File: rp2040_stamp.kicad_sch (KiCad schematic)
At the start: 38 parts, among them J1 Conn_South, J2 Conn_North, J3 Conn_East, J4 Conn_West, Q1 BSS84, SW1 SW_RESET, U1 RP2040, U2 AP2112K-3.3, U3 W25Q64JV, U4 MCP73831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

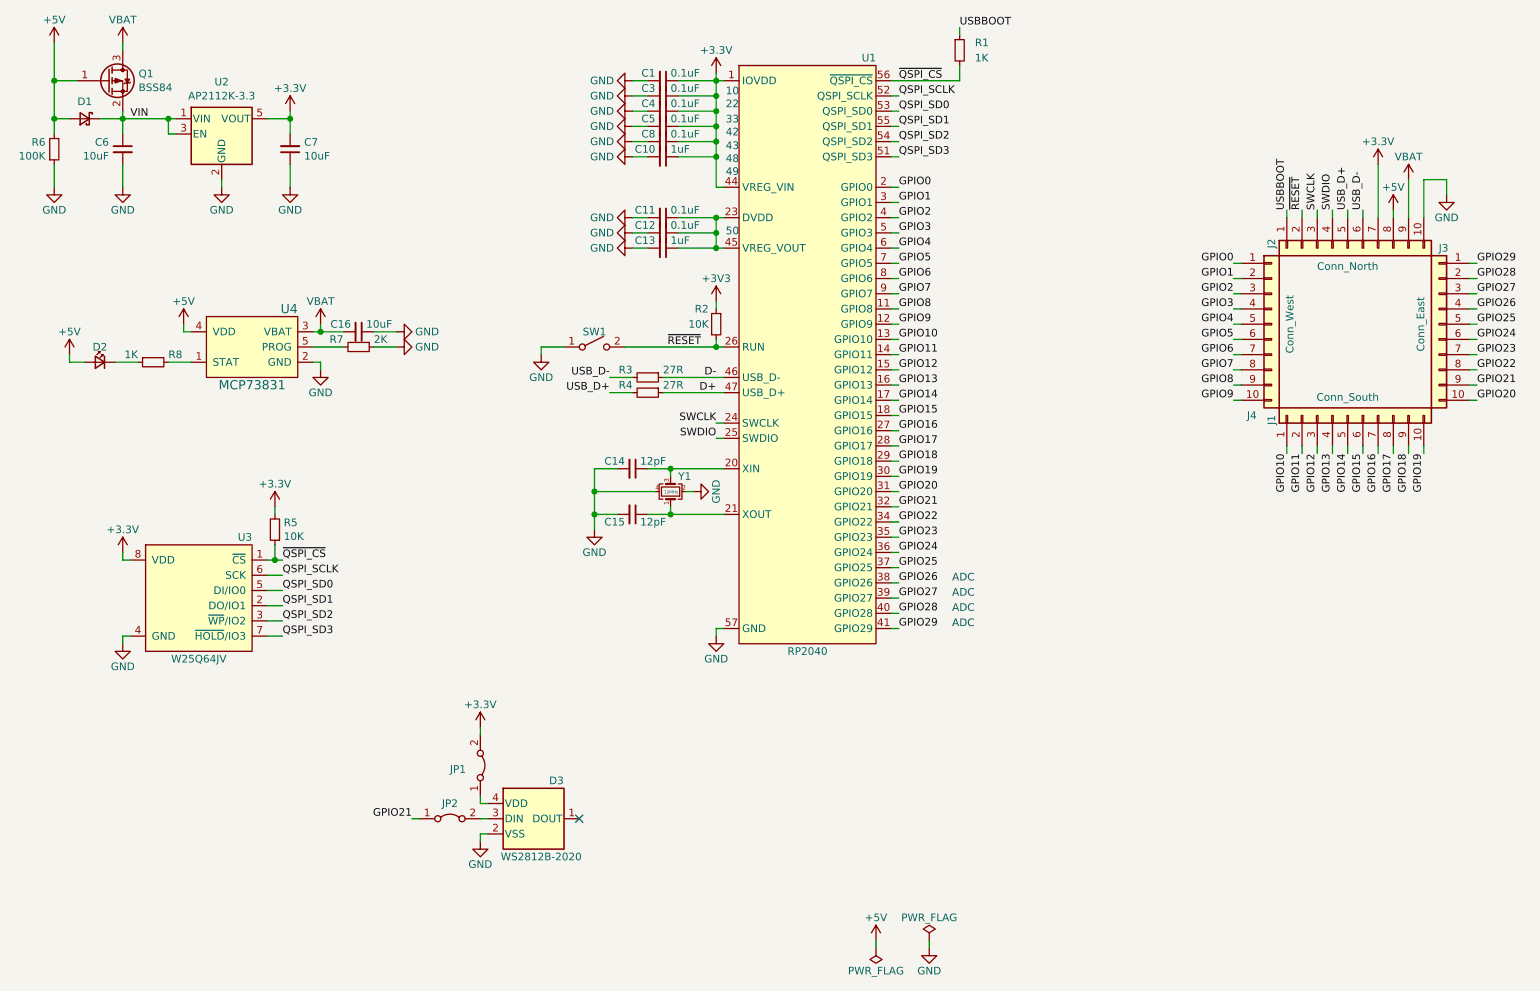
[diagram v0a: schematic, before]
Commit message: Removed unnecessary parts to be cheaper to manufacture via JLC.
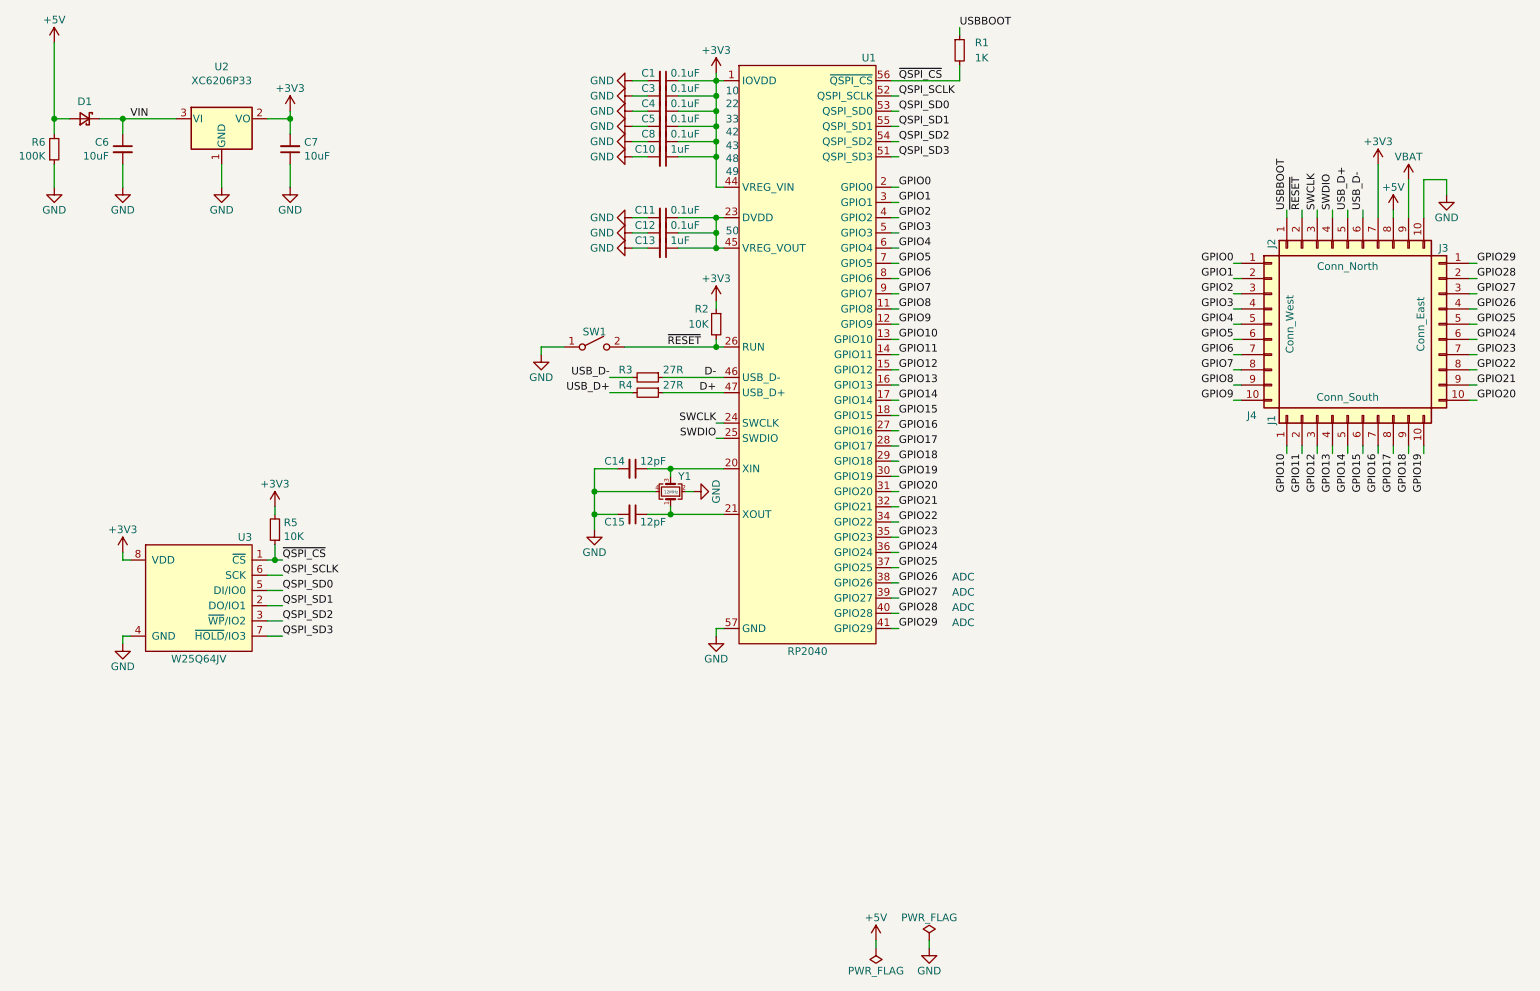
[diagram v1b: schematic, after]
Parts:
- removed C16: 10uF, Capacitor_SMD:C_0603_1608Metric, symbol Device:C_Small
- removed D2: LED_CHR, LED_SMD:LED_0603_1608Metric, symbol Device:LED_Small
- removed D3: WS2812B-2020, LED_SMD_Extra:WS2812B-2020, symbol LED_Extra:WS2812B-2020
- removed JP1: Jumper_Neopixel_VDD, Jumper:SolderJumper-2_P1.3mm_Bridged_RoundedPad1.0x1.5mm, symbol Jumper:Jumper_2_Bridged
- removed JP2: Jumper_Neopixel, Jumper:SolderJumper-2_P1.3mm_Bridged_RoundedPad1.0x1.5mm, symbol Jumper:Jumper_2_Bridged
- removed Q1: BSS84, Package_TO_SOT_SMD:SOT-23, symbol Transistor_FET:BSS84
- removed R7: 2K, Resistor_SMD:R_0603_1608Metric, symbol Device:R_Small
- removed R8: 1K, Resistor_SMD:R_0603_1608Metric, symbol Device:R_Small
- removed U4: MCP73831, Package_TO_SOT_SMD:SOT-23-5, symbol Battery_Management_Extra:MCP73831
- D1: LCSC C114023 -> C191023
- U2: value AP2112K-3.3 -> XC6206P33; footprint Package_TO_SOT_SMD:SOT-23-5 -> Package_TO_SOT_SMD:SOT-23-3; symbol Regulator_Linear:AP2112K-3.3 -> Regulator_Linear:XC6206PxxxMR; LCSC C51118 -> C5446
- U3: LCSC (none) -> C2940197
- Y1: footprint Crystal:Crystal_SMD_2520-4Pin_2.5x2.0mm -> Crystal:Crystal_SMD_3225-4Pin_3.2x2.5mm; LCSC C521567 -> C9002
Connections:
- net +3V3: now also U2.2 (VO); no longer U2.5 (VOUT)
- net GND: now also U2.1 (GND); no longer U2.2 (GND)
- net VIN: no longer U2.1 (VIN)
- net ~QSPI_CS~ renamed ~{QSPI_CS}
- net ~RESET~ renamed ~{RESET}
- no-connect marks 1 -> 0

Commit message: Created production files.
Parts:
- removed SW1: SW_RESET, Button_Switch_SMD:SW_SPST_B3U-1000P, symbol Switch:SW_SPST
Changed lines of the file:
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@@
 	)
 	(junction
-		(at 135.89 91.44)
+		(at 115.57 119.38)
 		(diameter 1.016)
 		(color 0 0 0 0)
 	)
 	(junction
-		(at 115.57 119.38)
-		(diameter 1.016)
+		(at 135.89 91.44)
+		(diameter 0)
 		(color 0 0 0 0)
 	)
@@
 	(wire
 		(pts
+			(xy 133.35 91.44) (xy 135.89 91.44)
+		)
+		(stroke
+			(width 0)
+			(type solid)
+		)
+	)
+	(wire
+		(pts
 			(xy 223.52 85.09) (xy 222.25 85.09)
 		)
@@
 	(wire
 		(pts
-			(xy 120.65 91.44) (xy 135.89 91.44)
-		)
-		(stroke
-			(width 0)
-			(type solid)
-		)
-	)
-	(wire
-		(pts
 			(xy 223.52 97.79) (xy 222.25 97.79)
 		)
@@
 	(wire
 		(pts
-			(xy 106.68 91.44) (xy 110.49 91.44)
-		)
-		(stroke
-			(width 0)
-			(type solid)
-		)
-	)
-	(wire
-		(pts
-			(xy 106.68 92.71) (xy 106.68 91.44)
-		)
-		(stroke
-			(width 0)
-			(type solid)
-		)
-	)
-	(wire
-		(pts
 			(xy 243.84 69.85) (xy 243.84 68.58)
 		)
@@
 	)
 	(symbol
-		(lib_id "power:GND")
-		(at 106.68 92.71 0)
-		(mirror y)
-		(unit 1)
-		(exclude_from_sim no)
-		(in_bom yes)
-		(on_board yes)
-		(dnp no)
-		(property "Reference" "#PWR0113"
-			(at 106.68 99.06 0)
-			(effects
-				(font
-					(size 1.27 1.27)
-				)
-				(hide yes)
-			)
-		)
-		(property "Value" "GND"
-			(at 106.68 96.52 0)
-			(effects
-				(font
-					(size 1.27 1.27)
-				)
-			)
-		)
-		(property "Footprint" ""
-			(at 106.68 92.71 0)
-			(effects
-				(font
-					(size 1.27 1.27)
-				)
-				(hide yes)
-			)
-		)
-		(property "Datasheet" ""
-			(at 106.68 92.71 0)
-			(effects
-				(font
-					(size 1.27 1.27)
-				)
-				(hide yes)
-			)
-		)
-		(property "Description" ""
-			(at 106.68 92.71 0)
-			(effects
-				(font
-					(size 1.27 1.27)
-				)
-				(hide yes)
-			)
-		)
-		(pin "1"
-		)
-		(instances
-			(project ""
-				(path "/872e912f-cc14-4edf-9f9a-f509de06f155"
-					(reference "#PWR0113")
-					(unit 1)
-				)
-			)
-		)
-	)
-	(symbol
 		(lib_id "power:+5V")
 		(at 162.56 190.5 0)
@@
 					(unit 1)
 				)
-			)
-		)
-	)
-	(symbol
-		(lib_id "Switch:SW_SPST")
-		(at 115.57 91.44 0)
-		(unit 1)
-		(exclude_from_sim no)
-		(in_bom yes)
-		(on_board yes)
-		(dnp no)
-		(property "Reference" "SW1"
-			(at 115.57 88.9 0)
-			(effects
-				(font
-					(size 1.27 1.27)
-				)
-			)
-		)
-		(property "Value" "SW_RESET"
-			(at 115.57 88.9 0)
-			(effects
-				(font
-					(size 1.27 1.27)
-				)
-				(hide yes)
-			)
-		)
-		(property "Footprint" "Button_Switch_SMD:SW_SPST_B3U-1000P"
-			(at 115.57 91.44 0)
-			(effects
-				(font
-					(size 1.27 1.27)
-				)
-				(hide yes)
-			)
-		)
-		(property "Datasheet" "~"
-			(at 115.57 91.44 0)
-			(effects
-				(font
-					(size 1.27 1.27)
-				)
-				(hide yes)
-			)
-		)
-		(property "Description" ""
-			(at 115.57 91.44 0)
-			(effects
-				(font
-					(size 1.27 1.27)
-				)
-				(hide yes)
-			)
-		)
-		(pin "1"
-		)
-		(pin "2"
-		)
-		(instances
-			(project ""
-				(path "/872e912f-cc14-4edf-9f9a-f509de06f155"
-					(reference "SW1")
-					(unit 1)
-				)
